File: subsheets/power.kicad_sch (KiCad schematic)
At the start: 58 parts, among them J1 USB_C_Receptacle_USB2.0, U1 CP2102N, U2 MCP73871_U, U3 LP2985-3.3, U4 LTC3525-5

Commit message: Generated more 3d models for pcb
-
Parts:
- J1: footprint Connector_USB:USB_C_Receptacle_Amphenol_12401610E4-2A -> Connector_USB:USB_C_Receptacle_XKB_U262-16XN-4BVC11
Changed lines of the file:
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@@
     (property "Reference" "J1" (id 0) (at 29.21 97.6335 0))
     (property "Value" "USB_C_Receptacle_USB2.0" (id 1) (at 29.21 100.4086 0))
-    (property "Footprint" "Connector_USB:USB_C_Receptacle_Amphenol_12401610E4-2A" (id 2) (at 33.02 119.38 0)
+    (property "Footprint" "Connector_USB:USB_C_Receptacle_XKB_U262-16XN-4BVC11" (id 2) (at 33.02 119.38 0)
       (effects (font (size 1.27 1.27)) hide)
     )

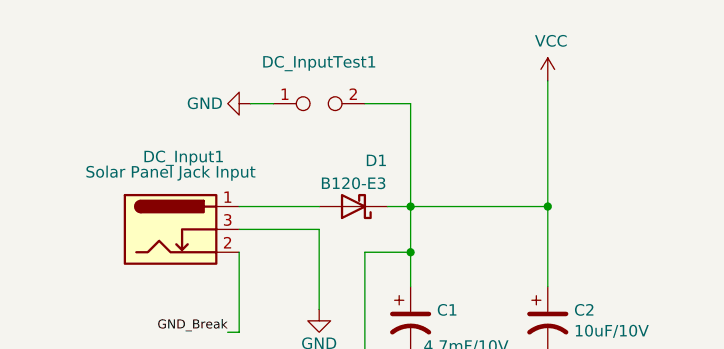
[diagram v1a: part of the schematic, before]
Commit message: Rearranged PCB for more efficient routing
-
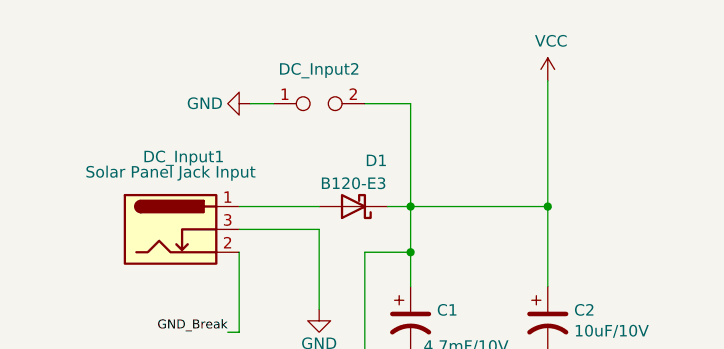
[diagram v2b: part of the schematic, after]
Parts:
- renumbered DC_InputTest1 to DC_Input2
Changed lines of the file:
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@@
   )
   (symbol (lib_id "Connector:TestPoint_2Pole") (at 48.26 25.4 0) (unit 1)
-    (in_bom yes) (on_board yes) (fields_autoplaced)
-    (property "Reference" "DC_InputTest1" (id 0) (at 48.26 20.7985 0))
+    (in_bom yes) (on_board yes)
+    (property "Reference" "DC_Input2" (id 0) (at 48.26 21.59 0))
     (property "Value" "TestPoint" (id 1) (at 48.26 23.5736 0)
       (effects (font (size 1.27 1.27)) hide)

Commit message: PCB Routed
-
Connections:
- net at D+1.1, D4.1 (A1), FL1.1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: now also J1.A6 (D+)
- net at D-1.1, D3.1 (A1), FL1.3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: now also J1.A7 (D-)
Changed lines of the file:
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@@
   (junction (at 105.41 99.06) (diameter 0) (color 0 0 0 0)
   )
+  (junction (at 46.99 124.46) (diameter 0) (color 0 0 0 0)
+  )
   (junction (at 191.77 29.21) (diameter 0) (color 0 0 0 0)
   )
@@
   )
   (junction (at 184.15 31.75) (diameter 0) (color 0 0 0 0)
+  )
+  (junction (at 46.99 119.38) (diameter 0) (color 0 0 0 0)
   )
   (junction (at 194.31 154.94) (diameter 0) (color 0 0 0 0)
@@
     (stroke (width 0) (type solid) (color 0 0 0 0))
   )
+  (wire (pts (xy 46.99 116.84) (xy 46.99 119.38))
+    (stroke (width 0) (type default) (color 0 0 0 0))
+  )
   (wire (pts (xy 126.365 144.78) (xy 128.905 144.78))
     (stroke (width 0) (type default) (color 0 0 0 0))
@@
     (stroke (width 0) (type default) (color 0 0 0 0))
   )
-  (wire (pts (xy 44.45 119.38) (xy 61.595 119.38))
+  (wire (pts (xy 44.45 119.38) (xy 46.99 119.38))
     (stroke (width 0) (type default) (color 0 0 0 0))
   )
@@
     (stroke (width 0) (type default) (color 0 0 0 0))
   )
+  (wire (pts (xy 46.99 119.38) (xy 61.595 119.38))
+    (stroke (width 0) (type default) (color 0 0 0 0))
+  )
   (wire (pts (xy 39.37 36.83) (xy 48.26 36.83))
     (stroke (width 0) (type default) (color 0 0 0 0))
@@
     (stroke (width 0) (type default) (color 0 0 0 0))
   )
+  (wire (pts (xy 46.99 121.92) (xy 46.99 124.46))
+    (stroke (width 0) (type default) (color 0 0 0 0))
+  )
   (wire (pts (xy 53.34 104.14) (xy 62.23 104.14))
     (stroke (width 0) (type default) (color 0 0 0 0))
@@
     (stroke (width 0) (type default) (color 0 0 0 0))
   )
+  (wire (pts (xy 44.45 116.84) (xy 46.99 116.84))
+    (stroke (width 0) (type default) (color 0 0 0 0))
+  )
   (wire (pts (xy 271.78 133.35) (xy 270.51 133.35))
     (stroke (width 0) (type default) (color 0 0 0 0))
@@
   )
   (wire (pts (xy 215.265 123.19) (xy 215.265 125.73))
+    (stroke (width 0) (type default) (color 0 0 0 0))
+  )
+  (wire (pts (xy 46.99 124.46) (xy 61.595 124.46))
     (stroke (width 0) (type default) (color 0 0 0 0))
   )
@@
     (stroke (width 0) (type default) (color 0 0 0 0))
   )
-  (wire (pts (xy 44.45 124.46) (xy 61.595 124.46))
+  (wire (pts (xy 44.45 124.46) (xy 46.99 124.46))
     (stroke (width 0) (type default) (color 0 0 0 0))
   )
@@
     (stroke (width 0) (type default) (color 0 0 0 0))
   )
+  (wire (pts (xy 44.45 121.92) (xy 46.99 121.92))
+    (stroke (width 0) (type default) (color 0 0 0 0))
+  )
